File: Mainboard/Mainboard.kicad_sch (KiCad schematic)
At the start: 27 parts, among them J1 Bus_M.2_Socket_E, J3 USB_A_Stacked, J4 Micro_SD_Card, J6 Conn_01x09_Pin, J7 Conn_01x09_Pin, U1 Hirose DF40C-100DS-0.4V, U2 ADS1115IDGS, U3 PCM5102, U4 PAM8403D

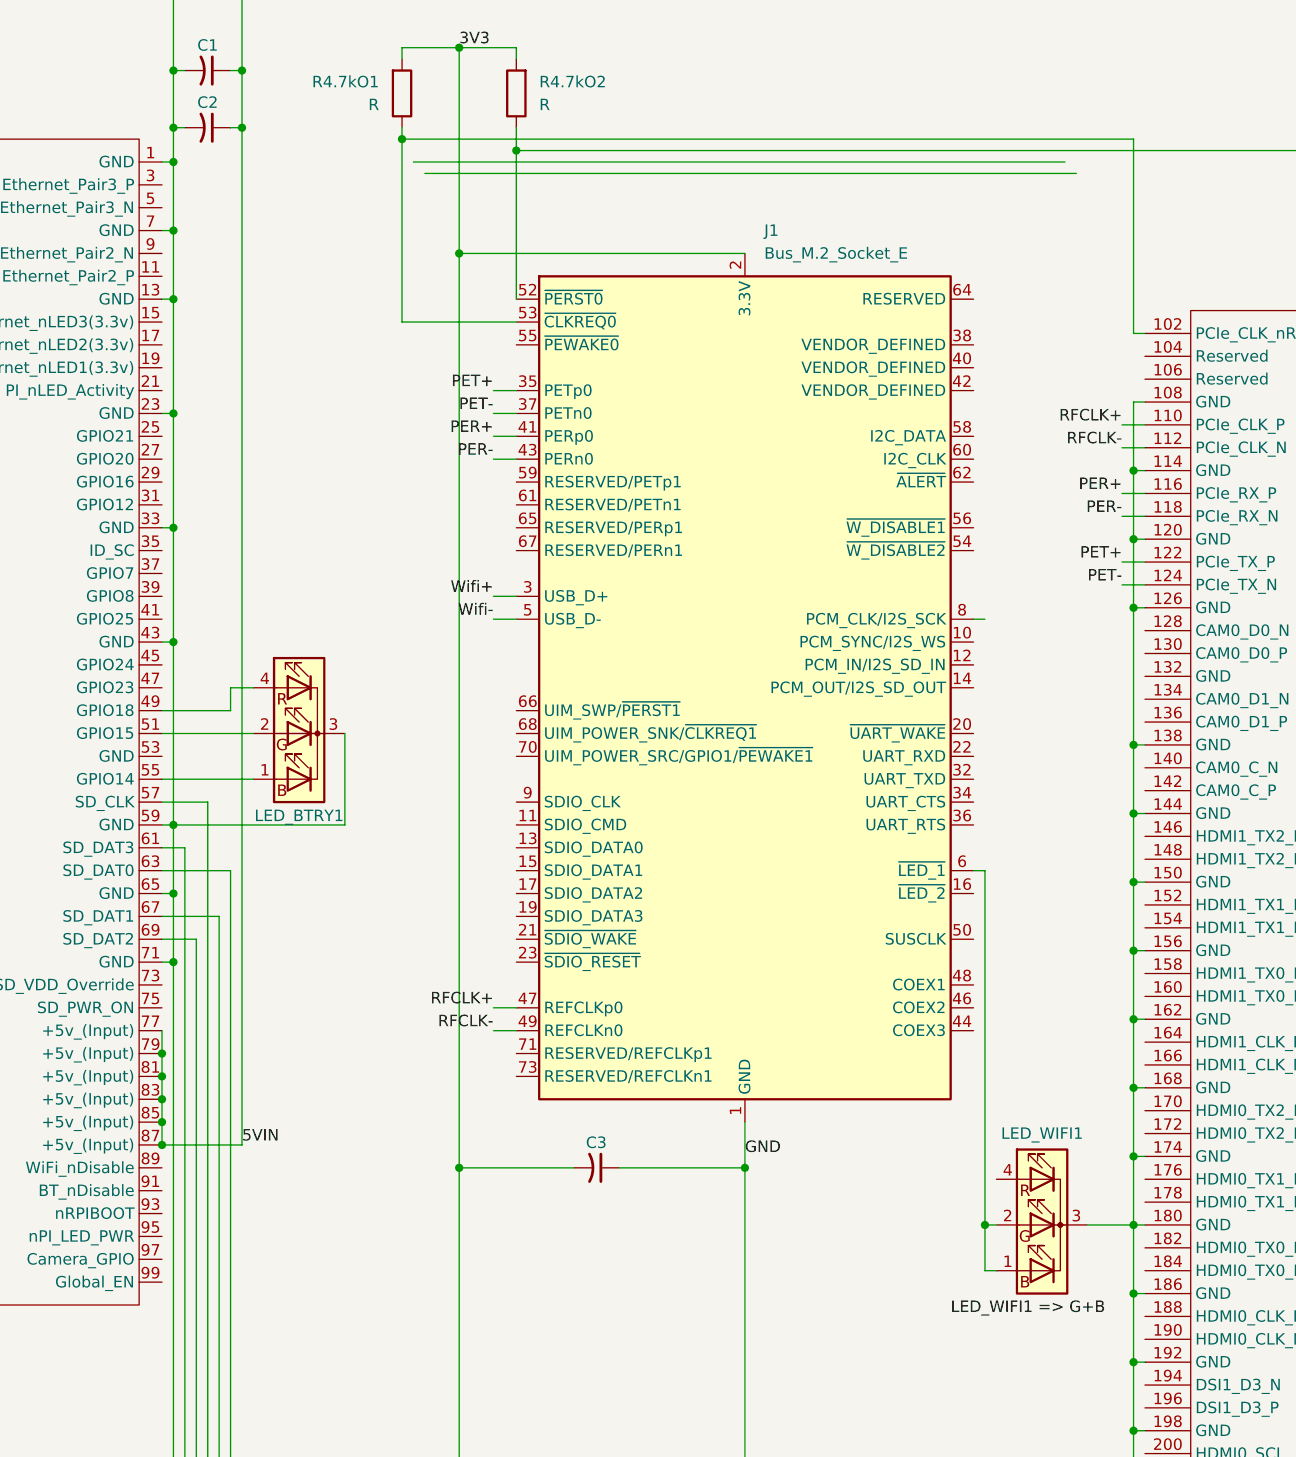
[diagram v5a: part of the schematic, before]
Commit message: Moved Wifi_LED to GPIO
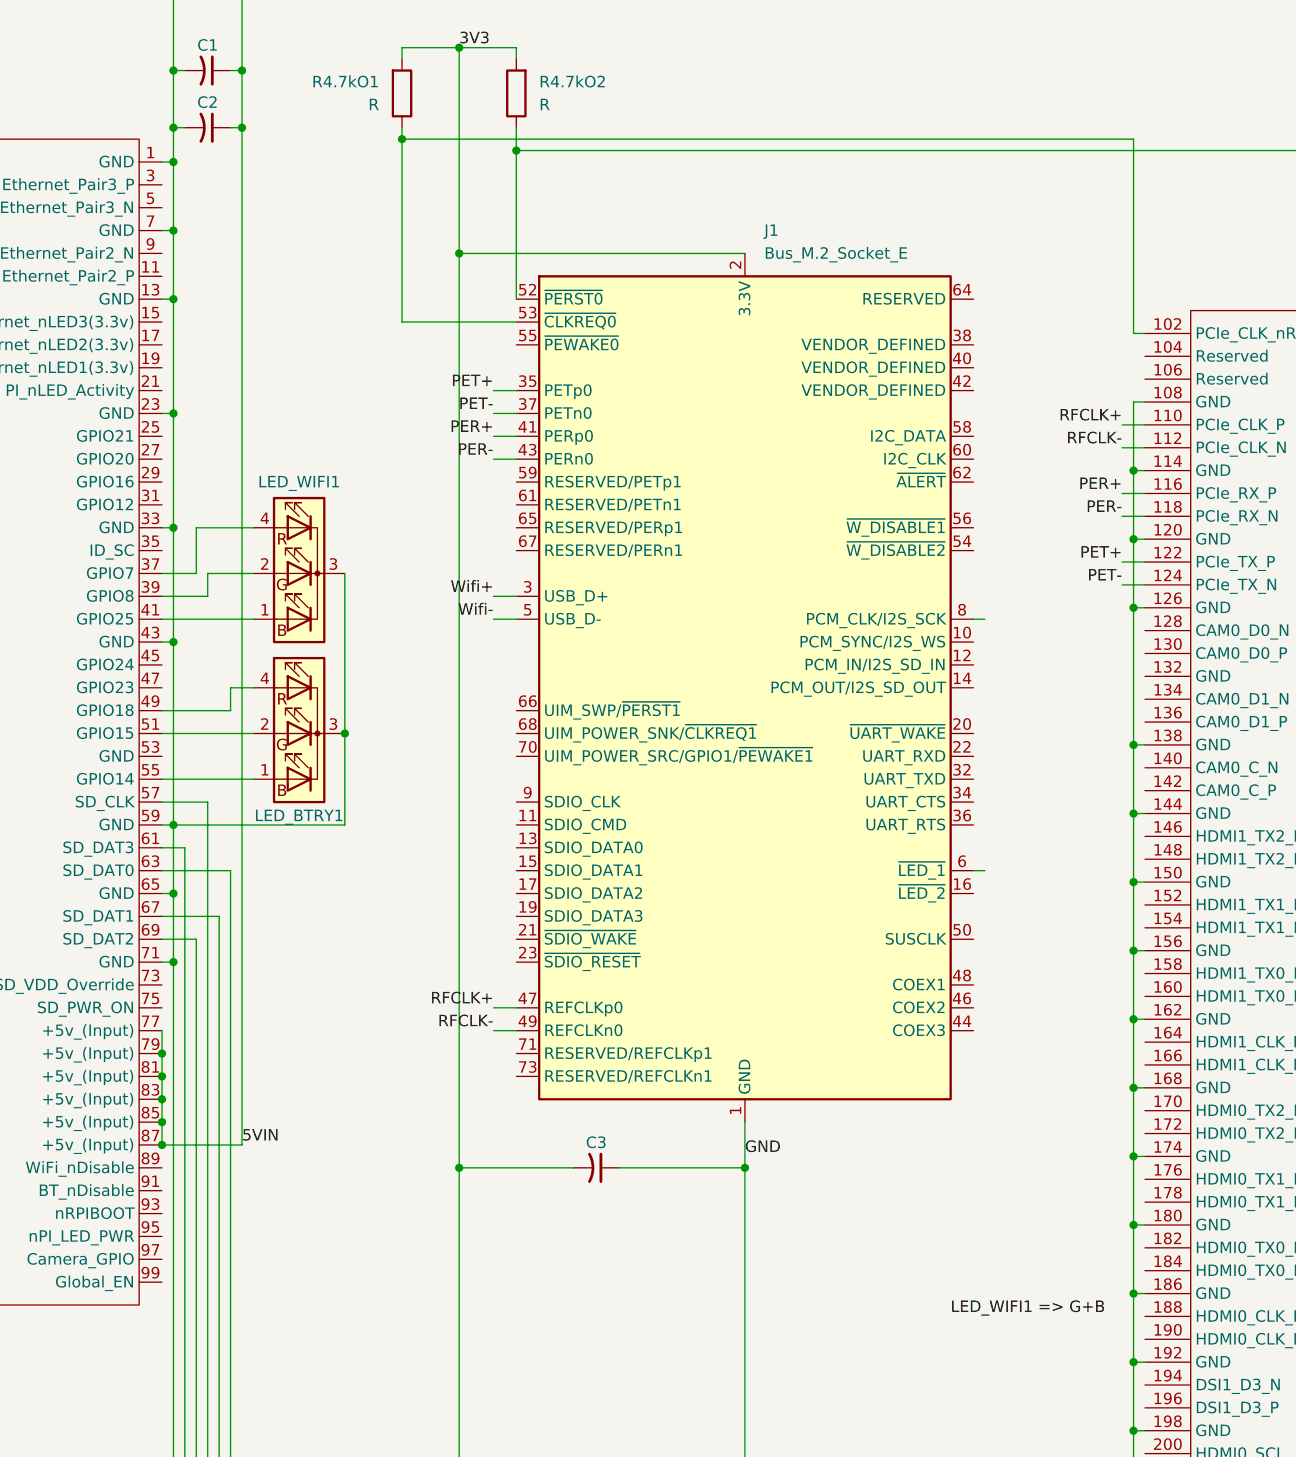
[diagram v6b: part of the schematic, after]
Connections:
- net at LED_WIFI1.4 (RA): now also U1.37 (GPIO7)
- net at U1.39 (GPIO8): now also LED_WIFI1.2 (GA)
- net at U1.41 (GPIO25): now also LED_WIFI1.1 (BA)
- now unconnected: J1.6 (~{LED_1})
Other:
- moved on the sheet: LED_WIFI1
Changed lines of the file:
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@@
 	)
 	(junction
-		(at 358.14 198.12)
-		(diameter 0)
-		(color 0 0 0 0)
-	)
-	(junction
 		(at 453.39 231.14)
 		(diameter 0)
@@
 	)
 	(junction
+		(at 287.02 143.51)
+		(diameter 0)
+		(color 0 0 0 0)
+	)
+	(junction
 		(at 374.65 121.92)
 		(diameter 0)
@@
 	(wire
 		(pts
+			(xy 271.78 128.27) (xy 266.7 128.27)
+		)
+		(stroke
+			(width 0)
+			(type default)
+		)
+	)
+	(wire
+		(pts
 			(xy 469.9 260.35) (xy 469.9 330.2)
 		)
@@
 	(wire
 		(pts
-			(xy 374.65 198.12) (xy 369.57 198.12)
-		)
-		(stroke
-			(width 0)
-			(type default)
-		)
-	)
-	(wire
-		(pts
 			(xy 363.22 312.42) (xy 363.22 302.26)
 		)
@@
 	(wire
 		(pts
-			(xy 287.02 143.51) (xy 287.02 153.67)
+			(xy 287.02 125.73) (xy 287.02 143.51)
 		)
 		(stroke
@@
 	(wire
 		(pts
+			(xy 287.02 143.51) (xy 287.02 153.67)
+		)
+		(stroke
+			(width 0)
+			(type default)
+		)
+	)
+	(wire
+		(pts
 			(xy 135.89 199.39) (xy 146.05 199.39)
 		)
@@
 	(wire
 		(pts
+			(xy 276.86 120.65) (xy 270.51 120.65)
+		)
+		(stroke
+			(width 0)
+			(type default)
+		)
+	)
+	(wire
+		(pts
 			(xy 274.32 251.46) (xy 196.85 251.46)
 		)
@@
 	(wire
 		(pts
-			(xy 367.03 80.01) (xy 294.64 80.01)
-		)
-		(stroke
-			(width 0)
-			(type default)
-		)
-	)
-	(wire
-		(pts
 			(xy 162.56 194.31) (xy 162.56 148.59)
 		)
@@
 	(wire
 		(pts
+			(xy 271.78 125.73) (xy 271.78 128.27)
+		)
+		(stroke
+			(width 0)
+			(type default)
+		)
+	)
+	(wire
+		(pts
 			(xy 467.36 372.11) (xy 469.9 372.11)
 		)
@@
 	(wire
 		(pts
+			(xy 266.7 130.81) (xy 276.86 130.81)
+		)
+		(stroke
+			(width 0)
+			(type default)
+		)
+	)
+	(wire
+		(pts
 			(xy 267.97 161.29) (xy 267.97 153.67)
 		)
@@
 	(wire
 		(pts
-			(xy 368.3 81.28) (xy 295.91 81.28)
-		)
-		(stroke
-			(width 0)
-			(type default)
-		)
-	)
-	(wire
-		(pts
 			(xy 453.39 170.18) (xy 436.88 170.18)
 		)
@@
 	(wire
 		(pts
-			(xy 358.14 158.75) (xy 358.14 198.12)
+			(xy 200.66 186.69) (xy 205.74 186.69)
 		)
 		(stroke
@@
 	(wire
 		(pts
-			(xy 200.66 186.69) (xy 205.74 186.69)
+			(xy 438.15 205.74) (xy 438.15 213.36)
 		)
 		(stroke
@@
 	(wire
 		(pts
-			(xy 438.15 205.74) (xy 438.15 213.36)
+			(xy 273.05 163.83) (xy 273.05 254)
 		)
 		(stroke
@@
 	(wire
 		(pts
-			(xy 273.05 163.83) (xy 273.05 254)
+			(xy 270.51 125.73) (xy 266.7 125.73)
 		)
 		(stroke
@@
 	(wire
 		(pts
-			(xy 359.41 203.2) (xy 358.14 203.2)
-		)
-		(stroke
-			(width 0)
-			(type default)
-		)
-	)
-	(wire
-		(pts
 			(xy 267.97 76.2) (xy 267.97 80.01)
 		)
@@
 	(wire
 		(pts
-			(xy 358.14 198.12) (xy 358.14 203.2)
-		)
-		(stroke
-			(width 0)
-			(type default)
-		)
-	)
-	(wire
-		(pts
 			(xy 331.47 186.69) (xy 331.47 191.77)
 		)
@@
 	(wire
 		(pts
-			(xy 443.23 238.76) (xy 463.55 238.76)
+			(xy 276.86 125.73) (xy 271.78 125.73)
 		)
 		(stroke
@@
 	(wire
 		(pts
-			(xy 436.88 182.88) (xy 438.15 182.88)
+			(xy 443.23 238.76) (xy 463.55 238.76)
 		)
 		(stroke
@@
 	(wire
 		(pts
-			(xy 438.15 228.6) (xy 438.15 236.22)
+			(xy 436.88 182.88) (xy 438.15 182.88)
 		)
 		(stroke
@@
 	(wire
 		(pts
-			(xy 358.14 198.12) (xy 359.41 198.12)
+			(xy 438.15 228.6) (xy 438.15 236.22)
 		)
 		(stroke
@@
 	(wire
 		(pts
+			(xy 270.51 120.65) (xy 270.51 125.73)
+		)
+		(stroke
+			(width 0)
+			(type default)
+		)
+	)
+	(wire
+		(pts
 			(xy 438.15 236.22) (xy 438.15 243.84)
 		)
@@
 	(symbol
 		(lib_id "Device:LED_BGKR")
-		(at 364.49 198.12 0)
+		(at 281.94 125.73 0)
 		(mirror y)
 		(unit 1)
@@
 		(dnp no)
 		(property "Reference" "LED_WIFI1"
-			(at 364.49 187.96 0)
+			(at 281.94 115.57 0)
 			(show_name no)
 			(do_not_autoplace no)
@@
 		)
 		(property "Value" "LED_BGKR"
-			(at 364.49 186.69 0)
+			(at 281.94 114.3 0)
 			(hide yes)
 			(show_name no)
@@
 		)
 		(property "Footprint" "LED_THT:LED_D5.0mm-4_RGB"
-			(at 364.49 199.39 0)
+			(at 281.94 127 0)
 			(hide yes)
 			(show_name no)
@@
 		)
 		(property "Datasheet" ""
-			(at 364.49 199.39 0)
+			(at 281.94 127 0)
 			(hide yes)
 			(show_name no)
@@
 		)
 		(property "Description" "RGB LED, blue/green/cathode/red"
-			(at 364.49 198.12 0)
+			(at 281.94 125.73 0)
 			(hide yes)
 			(show_name no)

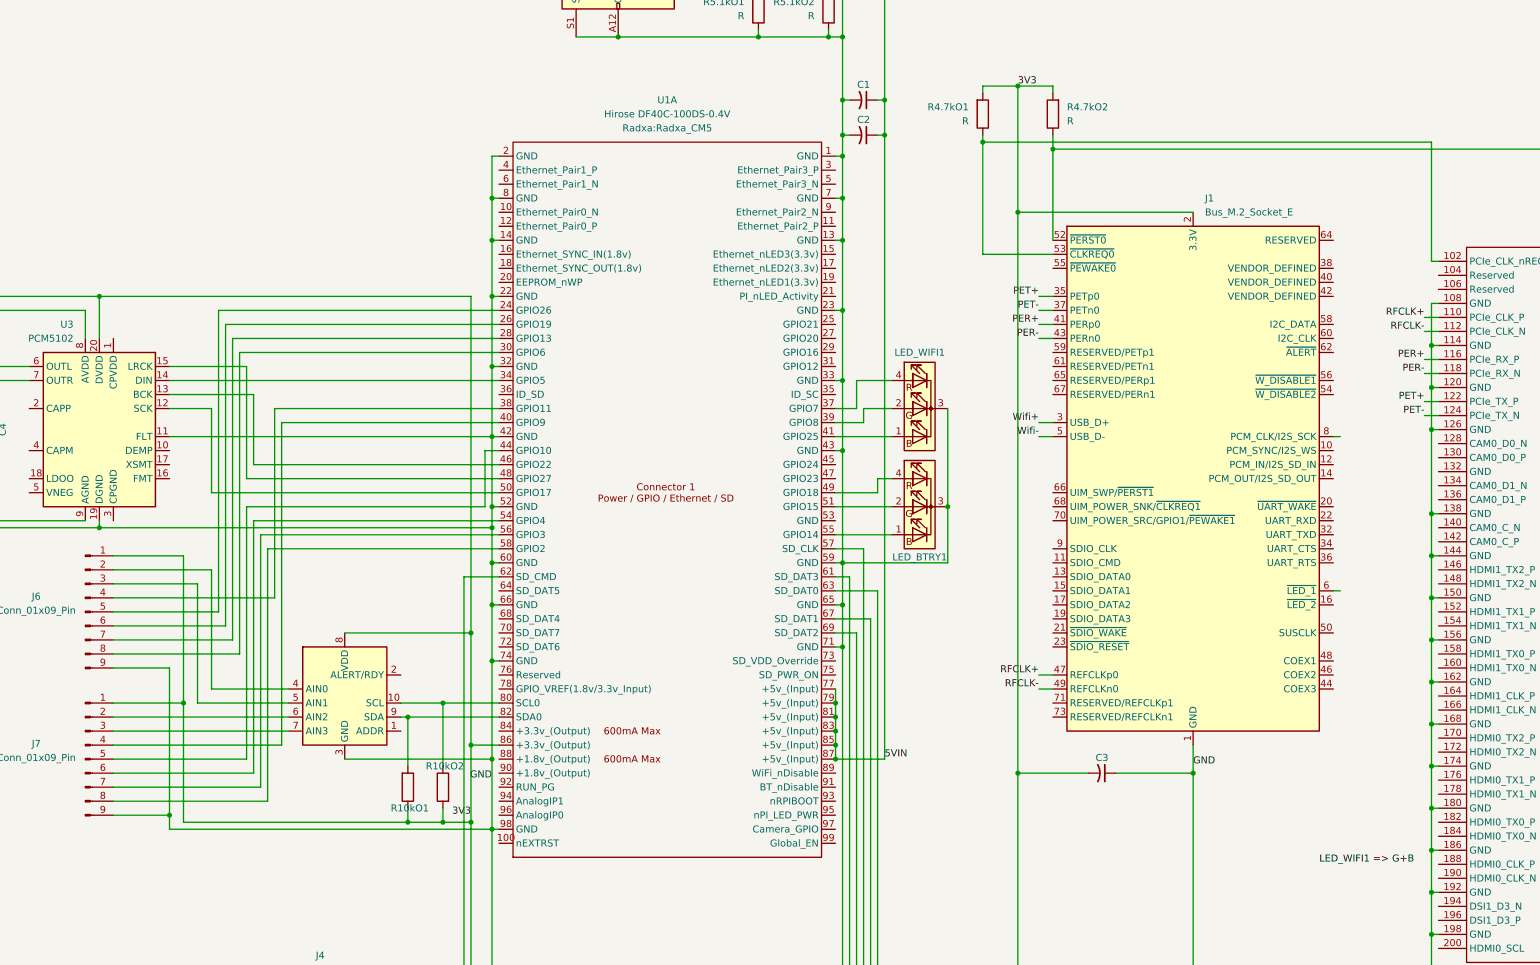
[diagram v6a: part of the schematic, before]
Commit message: Split Control Setup, -> L & R
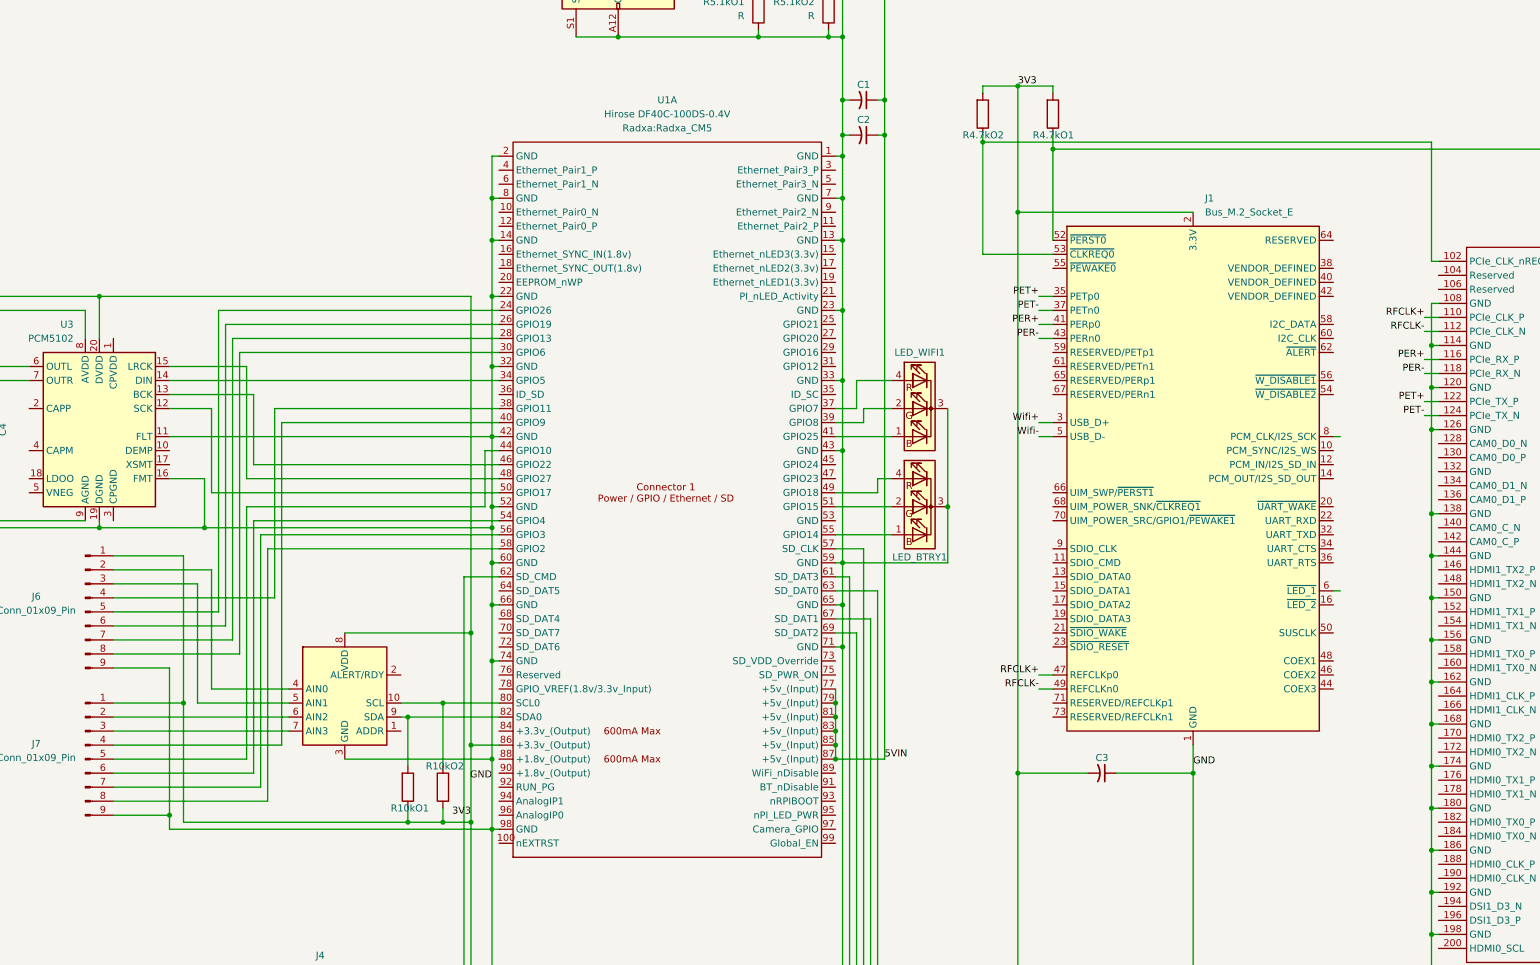
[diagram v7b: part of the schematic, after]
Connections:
- net GND: now also U3.16 (FMT)
- net at J1.53 (~{CLKREQ0}), U1.102 (PCIe_CLK_nREQ): now also R4.7kO2.1; no longer R4.7kO1.1
- net at J1.52 (~{PERST0}), U1.109 (PCIe_nRST): now also R4.7kO1.1; no longer R4.7kO2.1
